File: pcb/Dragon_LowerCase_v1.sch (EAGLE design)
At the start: 15 parts, among them IC1 2532, IC2 741LS61N, IC3 74LS00N, IC4 74LS244N, IC5 MC6847

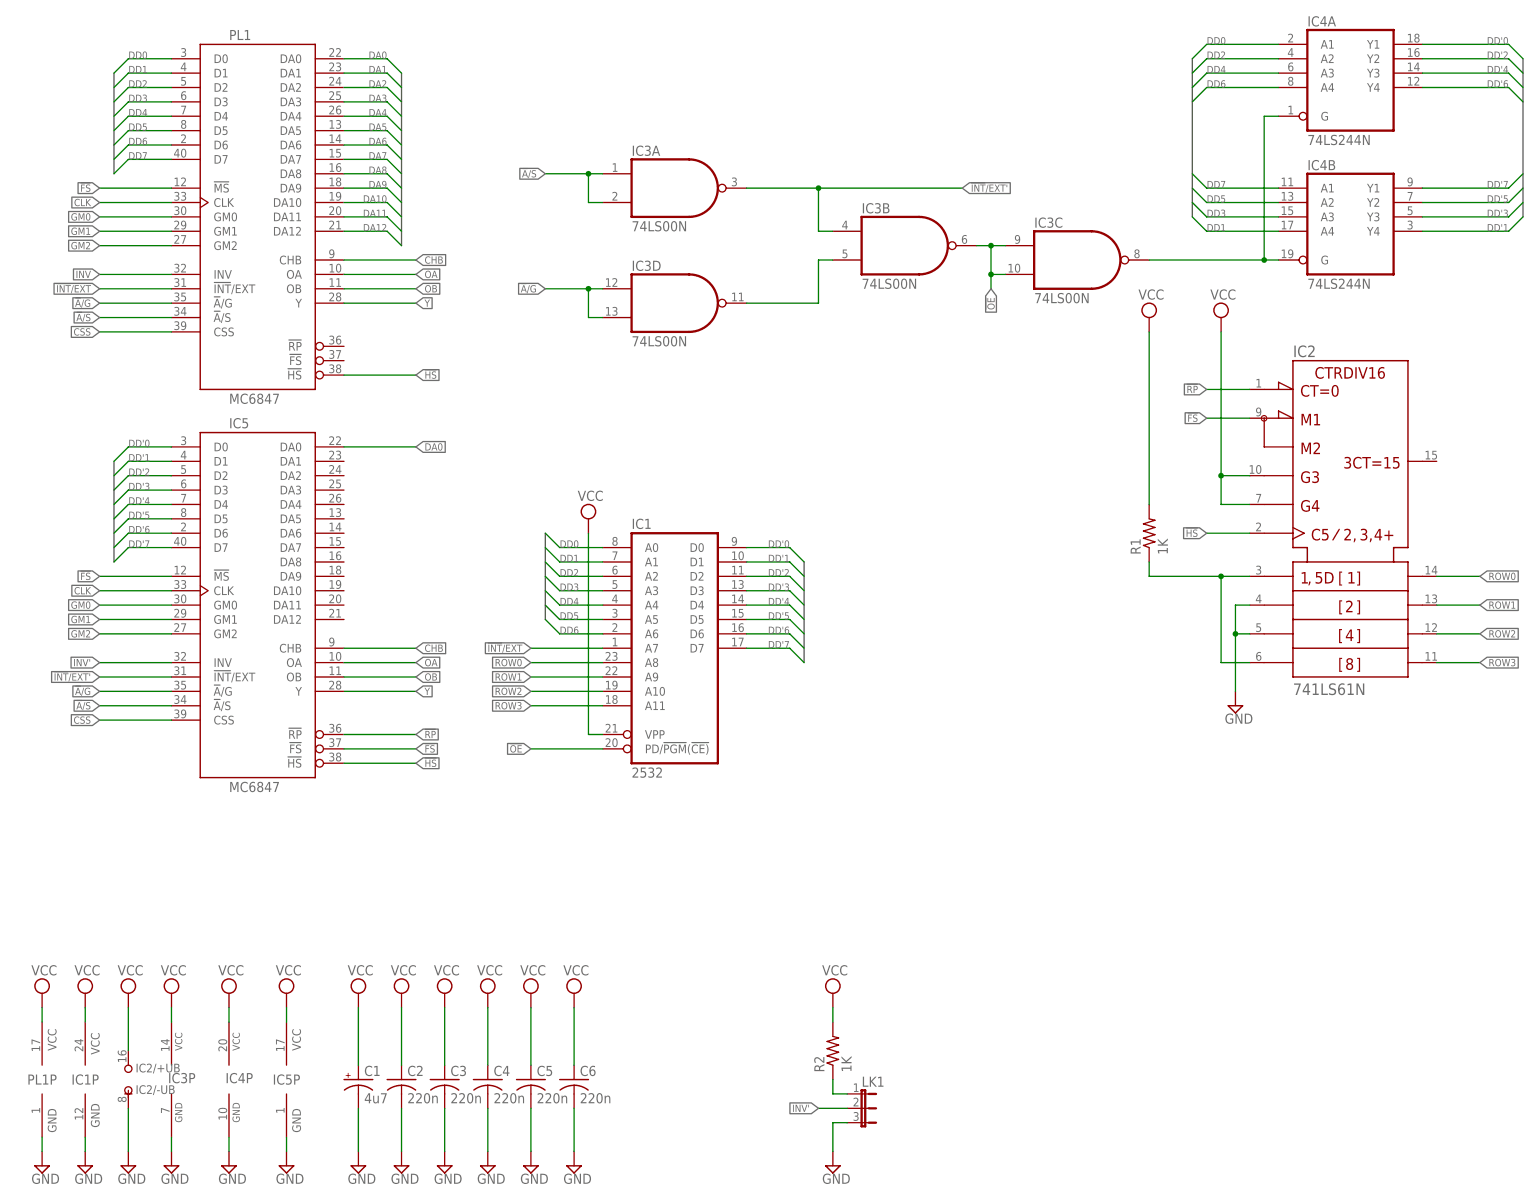
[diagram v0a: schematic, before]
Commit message: Shrink PCB and update EPROM. Add in reference data
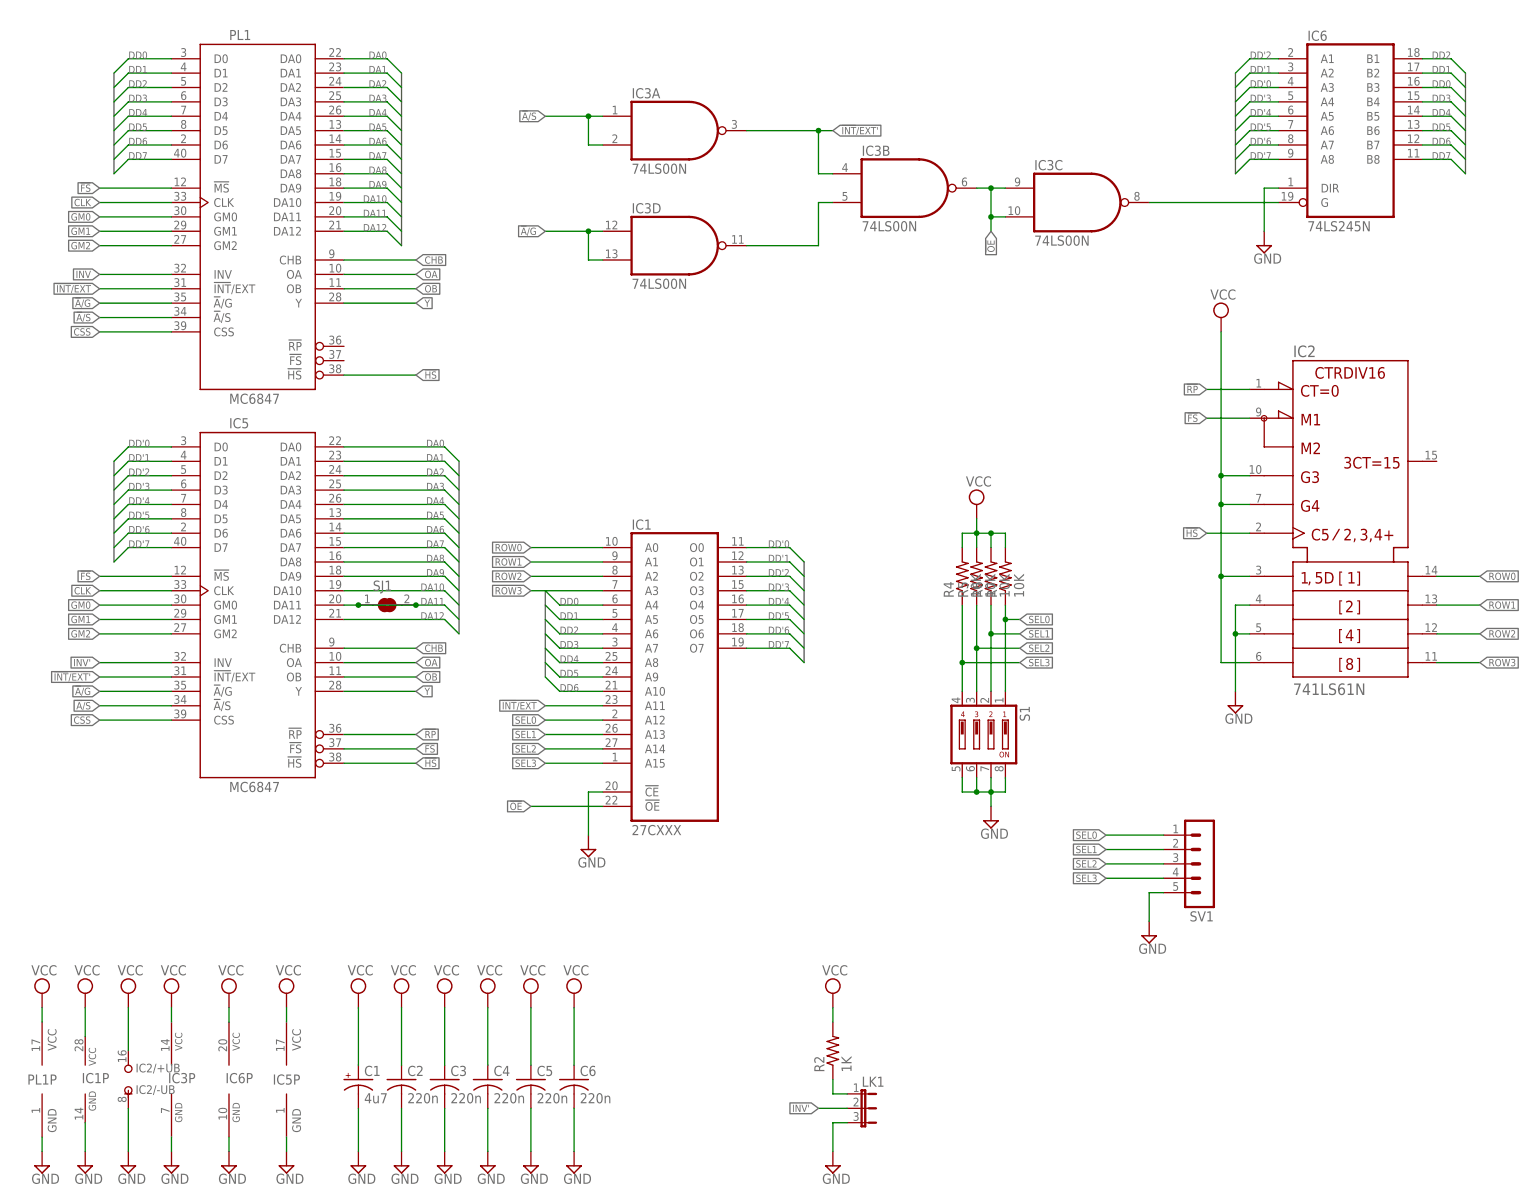
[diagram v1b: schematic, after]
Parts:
- removed IC4: 74LS244N, 74xx-us-jlb:74LS244N
- removed R1: 1K, resistor:R-US_0207/10
- added IC6: 74LS245N, 74xx-us-jlb:74LS245N
- added R4, R5, R6, R7: 10K, resistor:R-US_0204/2V
- added S1: (no value), switch-dil-rp:DS04
- added SJ1: (no value), jumper-jlb:SJ
- added SV1: (no value), con-lstb-rp:MA05-1
- C5: device resistor:C-US025-025X050 -> resistor:C-US050-025X075
- IC1: value 2532 -> 27CXXX; device memory-jlb:2532 -> memory-rp:27512
- R2: device resistor:R-US_0207/10 -> resistor:R-US_0204/2V
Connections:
- removed net N$1: IC21.A, IC21.D, R1.1
- removed net N$2: IC3C.O, IC4A.G, IC4B.G
- new net N$5: IC3C.O, IC6A.G
- new net SEL0: IC1A.A12, R7.1, S1.1, SV1.1
- new net SEL1: IC1A.A13, R6.1, S1.2, SV1.2
- new net SEL2: IC1A.A14, R5.1, S1.3, SV1.3
- new net SEL3: IC1A.A15, R4.1, S1.4, SV1.4
- net !INT!/EXT: now also IC1A.A11; no longer IC1A.A7
- net !OE: now also IC1A.!OE; no longer IC1A.PD/!PGM!(!CE)
- net DA1: now also IC5A.DA1
- net DA10: now also IC5A.DA10
- net DA11: now also IC5A.DA11, SJ1.1, SJ1.2
- net DA12: now also IC5A.DA12
- net DA2: now also IC5A.DA2
- net DA3: now also IC5A.DA3
- net DA4: now also IC5A.DA4
- net DA5: now also IC5A.DA5
- net DA6: now also IC5A.DA6
- net DA7: now also IC5A.DA7
- net DA8: now also IC5A.DA8
- net DA9: now also IC5A.DA9
- net DD'0: now also IC1A.O0, IC6A.A3; no longer IC1A.D0, IC4A.Y1
- net DD'1: now also IC1A.O1, IC6A.A2; no longer IC1A.D1, IC4B.Y4
- net DD'2: now also IC1A.O2, IC6A.A1; no longer IC1A.D2, IC4A.Y2
- net DD'3: now also IC1A.O3, IC6A.A4; no longer IC1A.D3, IC4B.Y3
- net DD'4: now also IC1A.O4, IC6A.A5; no longer IC1A.D4, IC4A.Y3
- net DD'5: now also IC1A.O5, IC6A.A6; no longer IC1A.D5, IC4B.Y2
- net DD'6: now also IC1A.O6, IC6A.A7; no longer IC1A.D6, IC4A.Y4
- net DD'7: now also IC1A.O7, IC6A.A8; no longer IC1A.D7, IC4B.Y1
- net DD0: now also IC1A.A4, IC6A.B3; no longer IC1A.A0, IC4A.A1
- net DD1: now also IC1A.A5, IC6A.B2; no longer IC1A.A1, IC4B.A4
- net DD2: now also IC1A.A6, IC6A.B1; no longer IC1A.A2, IC4A.A2
- net DD3: now also IC1A.A7, IC6A.B4; no longer IC1A.A3, IC4B.A3
- net DD4: now also IC1A.A8, IC6A.B5; no longer IC1A.A4, IC4A.A3
- net DD5: now also IC1A.A9, IC6A.B6; no longer IC1A.A5, IC4B.A2
- net DD6: now also IC1A.A10, IC6A.B7; no longer IC1A.A6, IC4A.A4
- net DD7: now also IC6A.B8; no longer IC4B.A1
- net GND: now also IC1A.!CE, IC6A.DIR, IC6P.GND, S1.5, S1.6, S1.7, S1.8, SV1.5; no longer IC4P.GND
- net ROW0: now also IC1A.A0; no longer IC1A.A8
- net ROW1: now also IC1A.A1; no longer IC1A.A9
- net ROW2: now also IC1A.A2; no longer IC1A.A10
- net ROW3: now also IC1A.A3; no longer IC1A.A11
- net VCC: now also IC21.A, IC21.D, IC6P.VCC, R4.2, R5.2, R6.2, R7.2; no longer IC1A.VPP, IC4P.VCC, R1.2
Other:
- moved on the sheet: IC3A, IC3B, IC3C, IC3D
